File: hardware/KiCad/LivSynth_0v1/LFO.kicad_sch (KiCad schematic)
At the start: 17 parts, among them Q5 2N3904, Q6 2N3904, Q7 2N3904, U2 TL074

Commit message: Initial Routing finished
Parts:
- added D9: LED, LED_THT:LED_D5.0mm, symbol Device:LED
- R24: value 470 -> 360
- RV4, RV5: footprint (none) -> SloBlo:RV141F-40-20BL
- U2: footprint (none) -> Package_SO:SOIC-14_3.9x8.7mm_P1.27mm
- U3: renamed from U2; footprint (none) -> Package_SO:SOIC-14_3.9x8.7mm_P1.27mm
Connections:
- net LFO_SQA_OUT: now also U3.1; no longer U3.8
- net LFO_TRI_OUT: now also U2.8; no longer U2.1
- net VGND: now also U2.10 (+), U2.13 (-), U3.3 (+); no longer U2.3 (+), U2.6 (-), U3.10 (+)
- net at R26.1, R28.2: now also U2.12 (+); no longer U2.5 (+)
- net at R26.2, R29.2, R30.1: now also U2.14, U3.2 (-); no longer U2.7, U3.9 (-)
- net at C33.1, RV4.2: now also U2.9 (-); no longer U2.2 (-)
- net at R24.2: now also D9.2 (A); no longer D6.2 (A)
- new net: D6.2 (A), D9.1 (K)
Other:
- note added: "R = (9-2*1.8)V/.015A = 360R"
- note removed: "R = (9-1.8)V/.015A ~= 470R"
- moved on the sheet: R24
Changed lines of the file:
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@@
   (junction (at 115.57 73.66) (diameter 0) (color 0 0 0 0)
   )
-  (wire (pts (xy 217.805 38.1) (xy 217.805 40.005))
+  (wire (pts (xy 217.805 30.48) (xy 217.805 32.385))
     (stroke (width 0) (type default) (color 0 0 0 0))
   )
@@
     (effects (font (size 1.27 1.27)) (justify left bottom))
   )
-  (text "R = (9-1.8)V/.015A ~= 470R" (at 228.6 43.815 0)
+  (text "R = (9-2*1.8)V/.015A = 360R" (at 228.6 43.815 0)
     (effects (font (size 1.27 1.27)) (justify left bottom))
   )
@@
     (effects (font (size 1.27 1.27)) (justify left))
   )
-  (symbol (lib_id "Amplifier_Operational:TL074") (at 154.94 78.74 0) (unit 2)
+  (symbol (lib_id "Amplifier_Operational:TL074") (at 154.94 78.74 0) (unit 4)
     (in_bom yes) (on_board yes)
     (property "Reference" "U2" (id 0) (at 154.94 69.85 0))
     (property "Value" "TL074" (id 1) (at 154.94 72.39 0))
-    (property "Footprint" "" (id 2) (at 153.67 76.2 0)
+    (property "Footprint" "Package_SO:SOIC-14_3.9x8.7mm_P1.27mm" (id 2) (at 153.67 76.2 0)
       (effects (font (size 1.27 1.27)) hide)
     )
@@
     (pin "2")
   )
-  (symbol (lib_id "Device:R") (at 217.805 43.815 0) (unit 1)
-    (in_bom yes) (on_board yes) (fields_autoplaced)
-    (property "Reference" "R24" (id 0) (at 219.71 42.5449 0)
+  (symbol (lib_id "Device:R") (at 217.805 36.195 0) (unit 1)
+    (in_bom yes) (on_board yes) (fields_autoplaced)
+    (property "Reference" "R24" (id 0) (at 219.71 34.9249 0)
       (effects (font (size 1.27 1.27)) (justify left))
     )
-    (property "Value" "470" (id 1) (at 219.71 45.0849 0)
+    (property "Value" "360" (id 1) (at 219.71 37.4649 0)
       (effects (font (size 1.27 1.27)) (justify left))
     )
-    (property "Footprint" "Resistor_THT:R_Axial_DIN0207_L6.3mm_D2.5mm_P7.62mm_Horizontal" (id 2) (at 216.027 43.815 90)
-      (effects (font (size 1.27 1.27)) hide)
-    )
-    (property "Datasheet" "~" (id 3) (at 217.805 43.815 0)
+    (property "Footprint" "Resistor_THT:R_Axial_DIN0207_L6.3mm_D2.5mm_P7.62mm_Horizontal" (id 2) (at 216.027 36.195 90)
+      (effects (font (size 1.27 1.27)) hide)
+    )
+    (property "Datasheet" "~" (id 3) (at 217.805 36.195 0)
       (effects (font (size 1.27 1.27)) hide)
     )
@@
       (effects (font (size 1.27 1.27)) (justify right))
     )
-    (property "Footprint" "" (id 2) (at 107.315 73.66 0)
+    (property "Footprint" "SloBlo:RV141F-40-20BL" (id 2) (at 107.315 73.66 0)
       (effects (font (size 1.27 1.27)) hide)
     )
@@
       (effects (font (size 1.27 1.27)) (justify right))
     )
-    (property "Footprint" "" (id 2) (at 165.1 117.475 0)
+    (property "Footprint" "SloBlo:RV141F-40-20BL" (id 2) (at 165.1 117.475 0)
       (effects (font (size 1.27 1.27)) hide)
     )
@@
     (pin "2")
   )
-  (symbol (lib_id "Amplifier_Operational:TL074") (at 125.095 76.2 0) (mirror x) (unit 1)
+  (symbol (lib_id "Amplifier_Operational:TL074") (at 125.095 76.2 0) (mirror x) (unit 3)
     (in_bom yes) (on_board yes)
     (property "Reference" "U2" (id 0) (at 125.095 67.31 0))
     (property "Value" "TL074" (id 1) (at 125.095 69.85 0))
-    (property "Footprint" "" (id 2) (at 123.825 78.74 0)
+    (property "Footprint" "Package_SO:SOIC-14_3.9x8.7mm_P1.27mm" (id 2) (at 123.825 78.74 0)
       (effects (font (size 1.27 1.27)) hide)
     )
@@
     (pin "3")
   )
-  (symbol (lib_id "Amplifier_Operational:TL074") (at 179.07 81.28 0) (mirror x) (unit 3)
+  (symbol (lib_id "Amplifier_Operational:TL074") (at 179.07 81.28 0) (mirror x) (unit 1)
     (in_bom yes) (on_board yes)
-    (property "Reference" "U2" (id 0) (at 179.07 72.39 0))
+    (property "Reference" "U3" (id 0) (at 179.07 72.39 0))
     (property "Value" "TL074" (id 1) (at 179.07 74.93 0))
-    (property "Footprint" "" (id 2) (at 177.8 83.82 0)
+    (property "Footprint" "Package_SO:SOIC-14_3.9x8.7mm_P1.27mm" (id 2) (at 177.8 83.82 0)
       (effects (font (size 1.27 1.27)) hide)
     )
@@
     (pin "4")
   )
-  (symbol (lib_id "power:+9V") (at 217.805 38.1 0) (unit 1)
-    (in_bom yes) (on_board yes) (fields_autoplaced)
-    (property "Reference" "#PWR044" (id 0) (at 217.805 41.91 0)
-      (effects (font (size 1.27 1.27)) hide)
-    )
-    (property "Value" "+9V" (id 1) (at 217.805 32.385 0))
-    (property "Footprint" "" (id 2) (at 217.805 38.1 0)
-      (effects (font (size 1.27 1.27)) hide)
-    )
-    (property "Datasheet" "" (id 3) (at 217.805 38.1 0)
-      (effects (font (size 1.27 1.27)) hide)
-    )
-    (pin "1")
+  (symbol (lib_id "power:+9V") (at 217.805 30.48 0) (unit 1)
+    (in_bom yes) (on_board yes) (fields_autoplaced)
+    (property "Reference" "#PWR044" (id 0) (at 217.805 34.29 0)
+      (effects (font (size 1.27 1.27)) hide)
+    )
+    (property "Value" "+9V" (id 1) (at 217.805 24.765 0))
+    (property "Footprint" "" (id 2) (at 217.805 30.48 0)
+      (effects (font (size 1.27 1.27)) hide)
+    )
+    (property "Datasheet" "" (id 3) (at 217.805 30.48 0)
+      (effects (font (size 1.27 1.27)) hide)
+    )
+    (pin "1")
+  )
+  (symbol (lib_id "Device:LED") (at 217.805 43.815 90) (unit 1)
+    (in_bom yes) (on_board yes) (fields_autoplaced)
+    (property "Reference" "D9" (id 0) (at 221.615 44.1324 90)
+      (effects (font (size 1.27 1.27)) (justify right))
+    )
+    (property "Value" "LED" (id 1) (at 221.615 46.6724 90)
+      (effects (font (size 1.27 1.27)) (justify right))
+    )
+    (property "Footprint" "LED_THT:LED_D5.0mm" (id 2) (at 217.805 43.815 0)
+      (effects (font (size 1.27 1.27)) hide)
+    )
+    (property "Datasheet" "~" (id 3) (at 217.805 43.815 0)
+      (effects (font (size 1.27 1.27)) hide)
+    )
+    (pin "1")
+    (pin "2")
   )
   (symbol (lib_id "Device:R") (at 133.985 100.33 90) (unit 1)

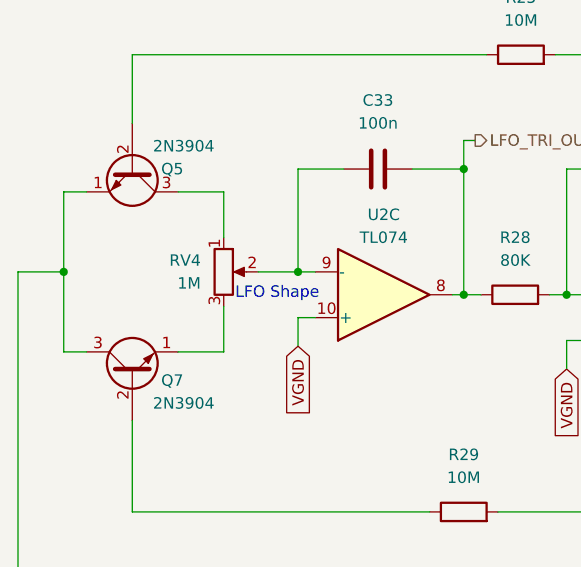
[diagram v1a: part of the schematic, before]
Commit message: Rework for polyester film capacitors
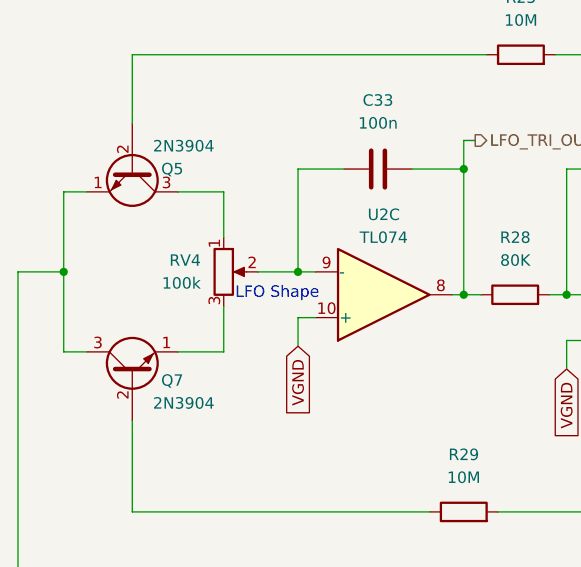
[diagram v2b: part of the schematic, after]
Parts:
- C33: footprint Capacitor_THT:C_Disc_D3.0mm_W1.6mm_P2.50mm -> Capacitor_THT:C_Rect_L7.2mm_W2.5mm_P5.00mm_FKS2_FKP2_MKS2_MKP2
- RV4: value 1M -> 100k
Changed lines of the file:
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@@
     (property "Reference" "C33" (id 0) (at 124.46 54.61 90))
     (property "Value" "100n" (id 1) (at 124.46 57.15 90))
-    (property "Footprint" "Capacitor_THT:C_Disc_D3.0mm_W1.6mm_P2.50mm" (id 2) (at 128.27 61.2648 0)
+    (property "Footprint" "Capacitor_THT:C_Rect_L7.2mm_W2.5mm_P5.00mm_FKS2_FKP2_MKS2_MKP2" (id 2) (at 128.27 61.2648 0)
       (effects (font (size 1.27 1.27)) hide)
     )
@@
       (effects (font (size 1.27 1.27)) (justify right))
     )
-    (property "Value" "1M" (id 1) (at 104.775 74.9299 0)
+    (property "Value" "100k" (id 1) (at 104.775 74.9299 0)
       (effects (font (size 1.27 1.27)) (justify right))
     )

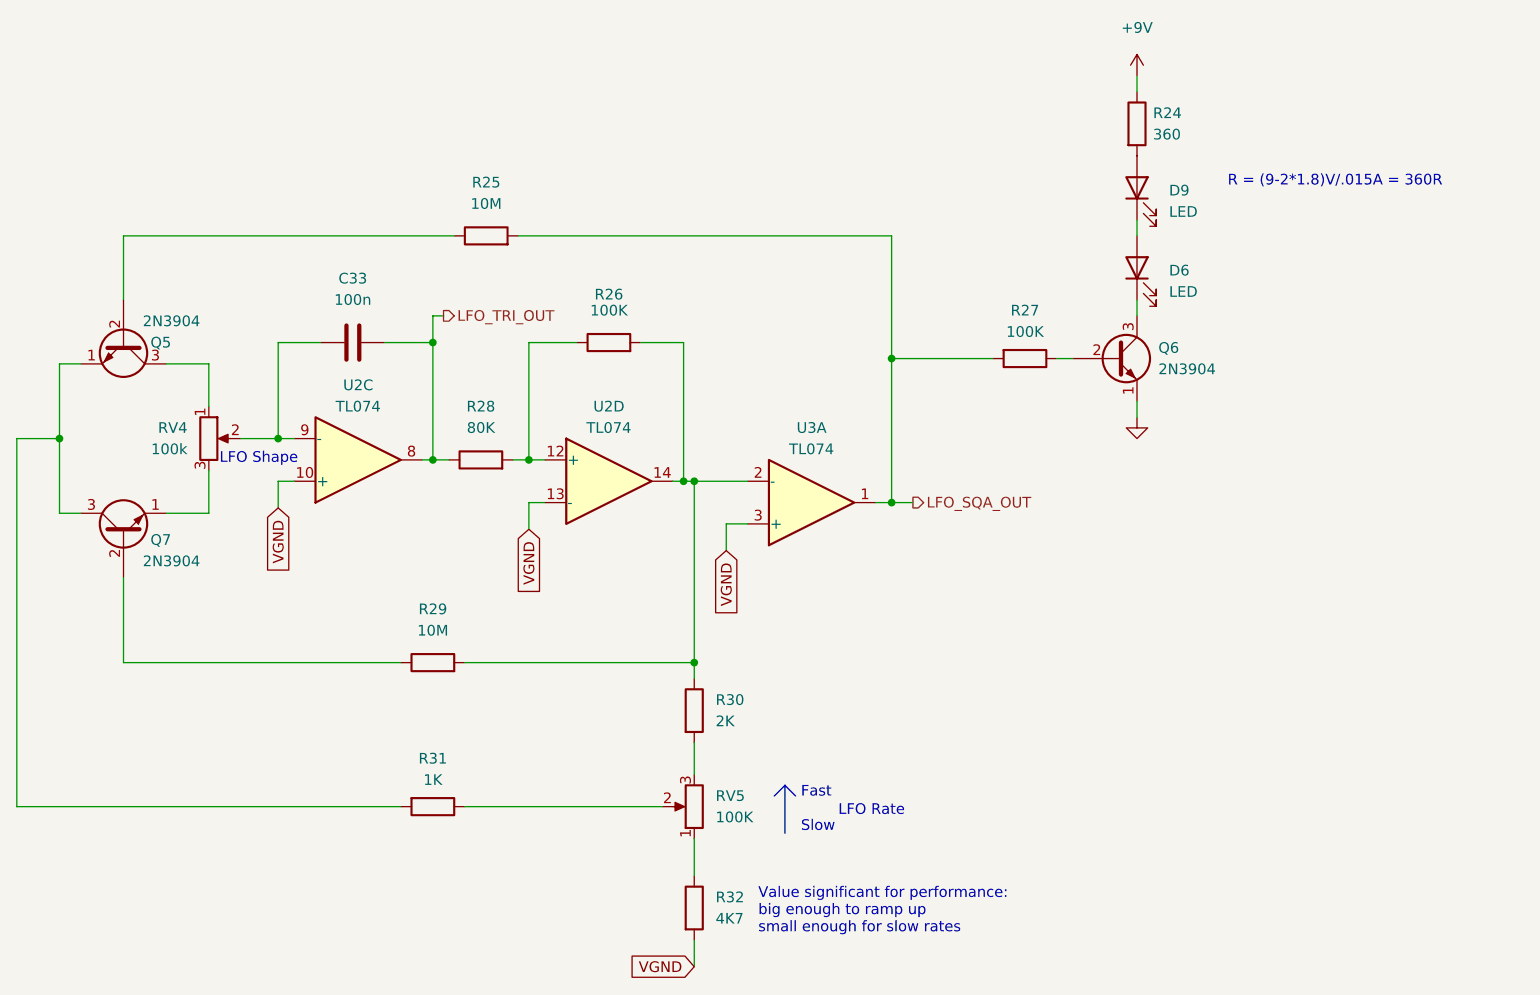
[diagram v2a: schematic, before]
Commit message: Change LED status circuits
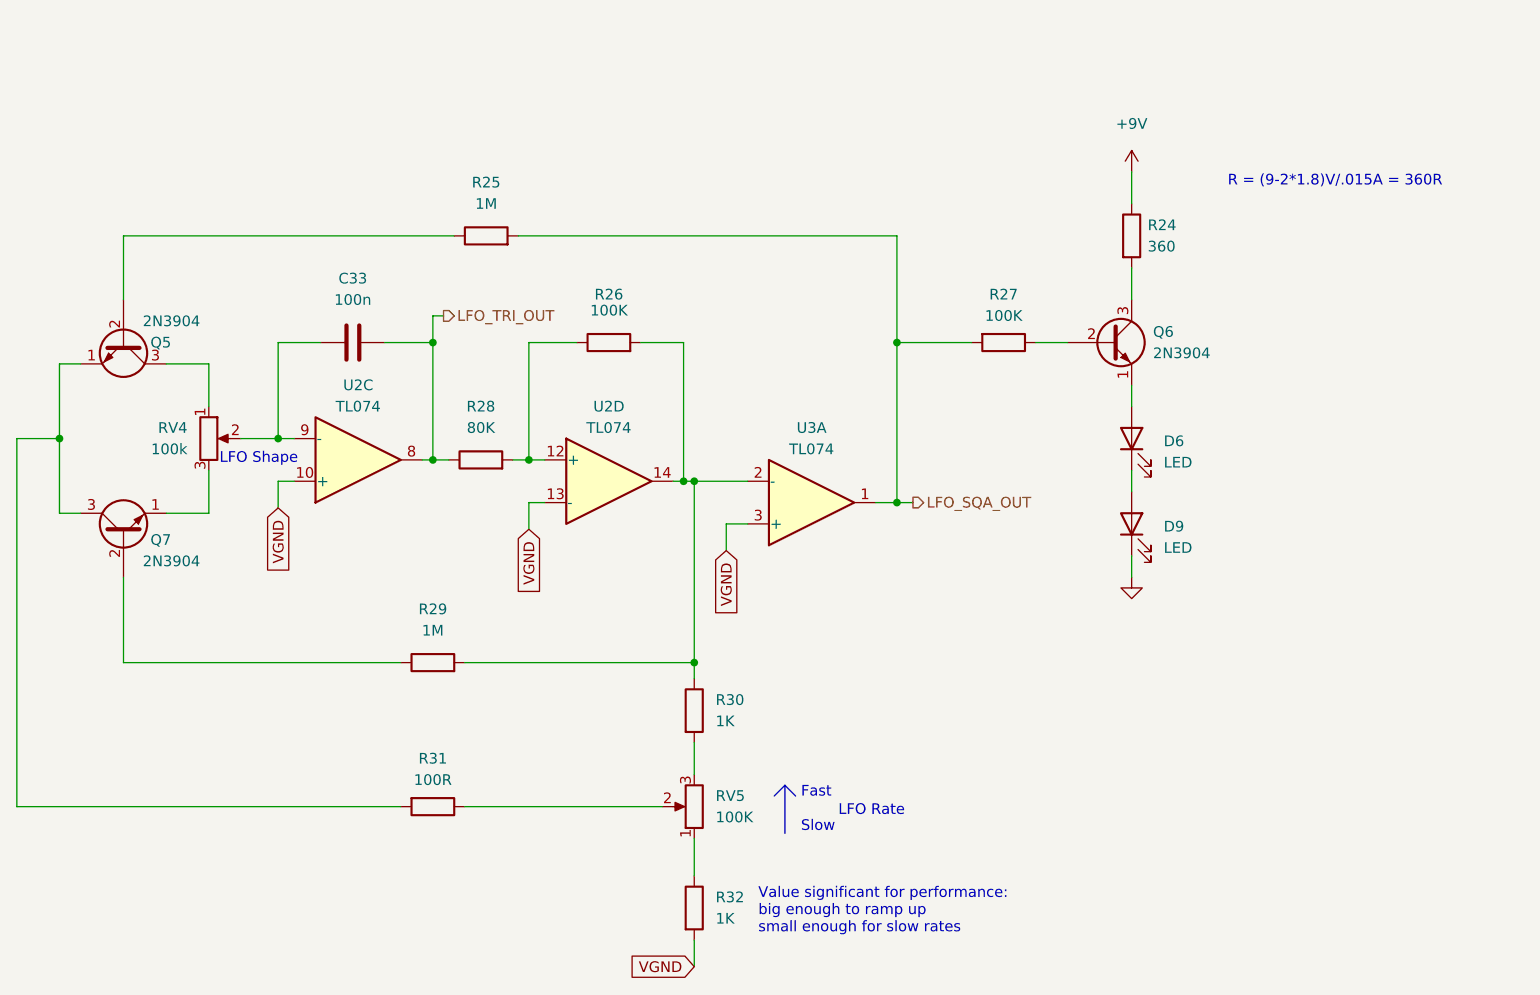
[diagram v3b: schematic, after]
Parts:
- R25, R29: value 10M -> 1M
- R30: value 2K -> 1K
- R31: value 1K -> 100R
- R32: value 4K7 -> 1K
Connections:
- net GND: now also D9.1 (K); no longer Q6.1 (E)
- net at R24.2: now also Q6.3 (C); no longer D9.2 (A)
- net at D6.1 (K): now also D9.2 (A); no longer Q6.3 (C)
- net at D6.2 (A): now also Q6.1 (E); no longer D9.1 (K)
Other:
- moved on the sheet: D6, D9, Q6, R24, R27

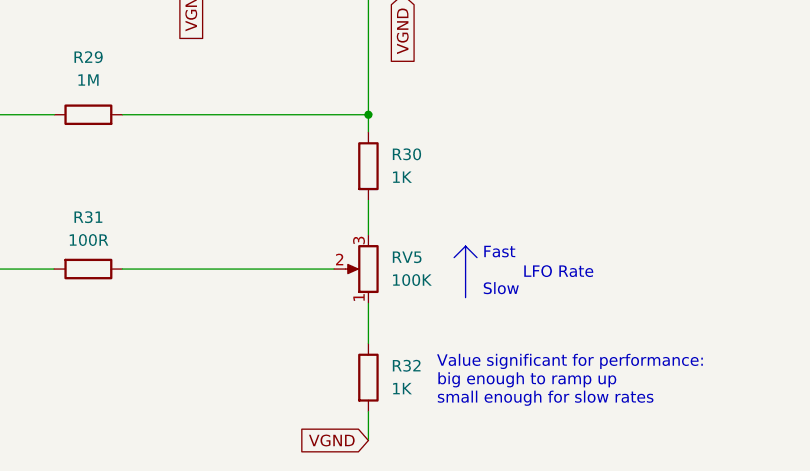
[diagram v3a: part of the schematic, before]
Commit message: White balance for RGB LEDs
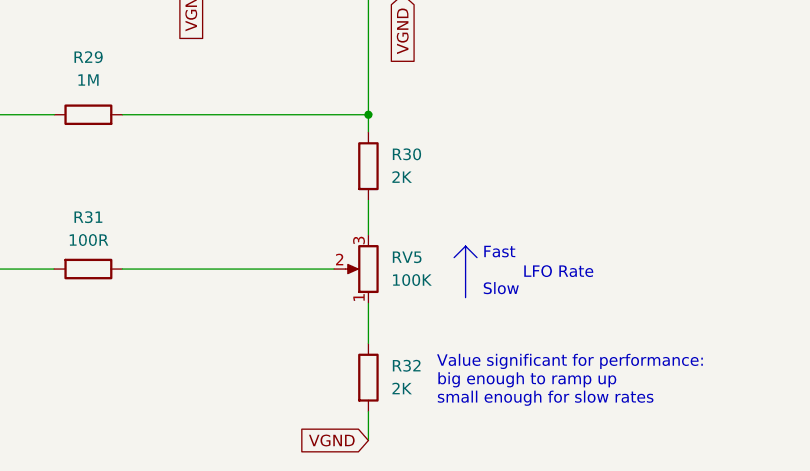
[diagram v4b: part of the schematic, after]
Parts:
- R30, R32: value 1K -> 2K
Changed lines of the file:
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@@
       (effects (font (size 1.27 1.27)) (justify left))
     )
-    (property "Value" "1K" (id 1) (at 167.64 130.8099 0)
+    (property "Value" "2K" (id 1) (at 167.64 130.8099 0)
       (effects (font (size 1.27 1.27)) (justify left))
     )
@@
       (effects (font (size 1.27 1.27)) (justify left))
     )
-    (property "Value" "1K" (id 1) (at 167.64 107.3149 0)
-      (effects (font (size 1.27 1.27)) (justify left))
-    )
+    (property "Value" "2K" (id 1) (at 167.64 107.3149 0)
+      (effects (font (size 1.27 1.27)) (justify left))
+    )
